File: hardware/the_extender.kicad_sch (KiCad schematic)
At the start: 122 parts, among them J0 TYPE-C 24P QT 143, J1 TYPE-C-31-M-16, J2 U231-091N-3BLRC11, J3 PJ-327D-5A, J4 PJ-327D-5A, J5 AF 10.0 HC6.3, Q4 SSM3J332R,LF, Q6 SSM3J332R,LF, U0 RT6150BGQW, U1 IP5306-I2C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

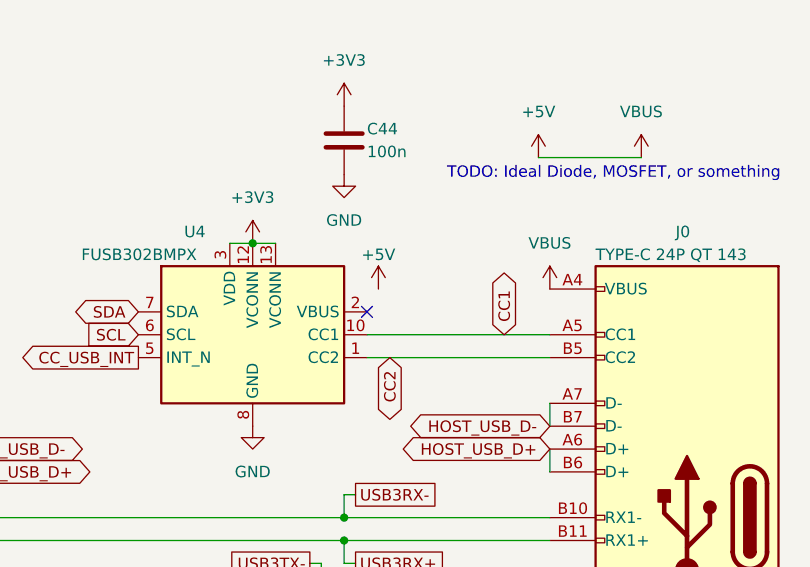
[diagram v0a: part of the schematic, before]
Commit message: reconnect VBUS to FUSB302
i think its needed for the pullups
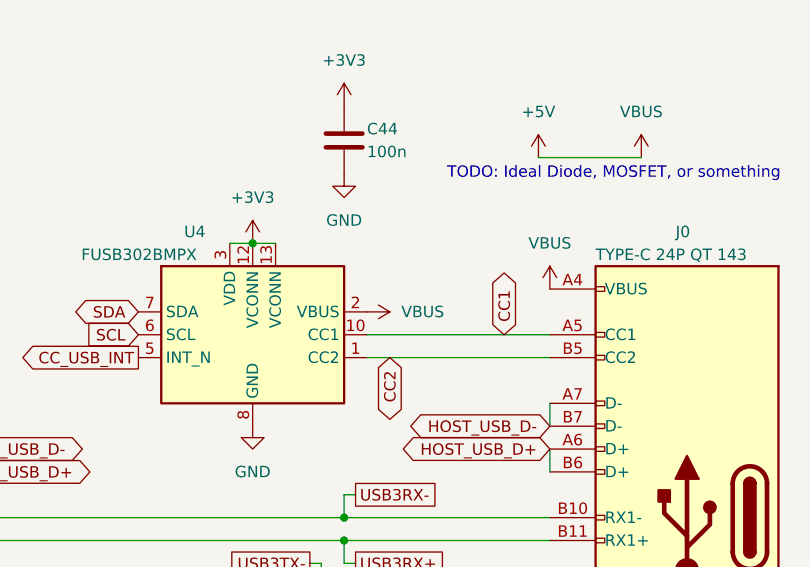
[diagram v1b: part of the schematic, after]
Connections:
- net +5V: now also U4.2 (VBUS)
- no-connect marks 50 -> 49
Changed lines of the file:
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@@
   (no_connect (at 374.65 146.05))
   (no_connect (at 60.96 137.16))
-  (no_connect (at 104.14 46.99))
   (no_connect (at 374.65 74.93))
   (no_connect (at 374.65 138.43))
@@
     )
   )
-  (symbol (lib_id "power:+5V") (at 105.41 44.45 0) (unit 1)
-    (in_bom yes) (on_board yes) (dnp no)
-    (property "Reference" "#PWR0108" (at 105.41 48.26 0)
-      (effects (font (size 1.27 1.27)) hide)
-    )
-    (property "Value" "+5V" (at 105.41 40.64 0)
-      (effects (font (size 1.27 1.27)))
-    )
-    (property "Footprint" "" (at 105.41 44.45 0)
-      (effects (font (size 1.27 1.27)) hide)
-    )
-    (property "Datasheet" "" (at 105.41 44.45 0)
-      (effects (font (size 1.27 1.27)) hide)
-    )
-    (pin "1")
-    (instances
-      (project "the_extender"
-        (path "/e63e39d7-6ac0-4ffd-8aa3-1841a4541b55"
-          (reference "#PWR0108") (unit 1)
-        )
-      )
-    )
-  )
   (symbol (lib_id "Device:R") (at 355.6 53.34 90) (unit 1)
     (in_bom yes) (on_board yes) (dnp no)
@@
         )
       )
+    )
+  )
+  (symbol (lib_id "power:VBUS") (at 104.14 46.99 270) (unit 1)
+    (in_bom yes) (on_board yes) (dnp no) (fields_autoplaced)
+    (property "Reference" "#PWR082" (at 100.33 46.99 0)
+      (effects (font (size 1.27 1.27)) hide)
+    )
+    (property "Value" "VBUS" (at 107.95 46.99 90)
+      (effects (font (size 1.27 1.27)) (justify left))
+    )
+    (property "Footprint" "" (at 104.14 46.99 0)
+      (effects (font (size 1.27 1.27)) hide)
+    )
+    (property "Datasheet" "" (at 104.14 46.99 0)
+      (effects (font (size 1.27 1.27)) hide)
+    )
+    (pin "1")
+    (instances
+      (project "the_extender"
+        (path "/e63e39d7-6ac0-4ffd-8aa3-1841a4541b55"
+          (reference "#PWR082") (unit 1)
+        )
+      )

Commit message: switch 3v3 footprint, fixup stuff
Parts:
- U0: value RT6150BGQW -> RT6150AGQW; footprint Package_SON:WSON-10-1EP_2.5x2.5mm_P0.5mm_EP1.2x2mm -> Package_DFN_QFN:WDFN-10-1EP_3x3mm_P0.5mm_EP1.8x2.5mm
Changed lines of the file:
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@@
       (effects (font (size 1.27 1.27)))
     )
-    (property "Value" "RT6150BGQW" (at 354.33 215.9 0)
+    (property "Value" "RT6150AGQW" (at 354.33 215.9 0)
       (effects (font (size 1.27 1.27)))
     )
-    (property "Footprint" "Package_SON:WSON-10-1EP_2.5x2.5mm_P0.5mm_EP1.2x2mm" (at 354.33 241.3 0)
+    (property "Footprint" "Package_DFN_QFN:WDFN-10-1EP_3x3mm_P0.5mm_EP1.8x2.5mm" (at 354.33 241.3 0)
       (effects (font (size 1.27 1.27)) hide)
     )

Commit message: switch to cheaper and smaller usb hub, part 1
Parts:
- removed R15: 12k, Resistor_SMD:R_0805_2012Metric_Pad1.20x1.40mm_HandSolder, symbol Device:R
- removed R17, R33: 10k, Resistor_SMD:R_0805_2012Metric_Pad1.20x1.40mm_HandSolder, symbol Device:R
- removed U5: USB2514B_Bi, Package_DFN_QFN:QFN-36-1EP_6x6mm_P0.5mm_EP3.7x3.7mm, symbol Interface_USB:USB2514B_Bi
- added JP2, JP3: SolderJumper_2_Open, symbol Jumper:SolderJumper_2_Open
- added U5: ~, Package_DFN_QFN:QFN-24-1EP_4x4mm_P0.5mm_EP2.6x2.6mm, symbol H3_IC:CH334F
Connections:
- net +3.3VP: now also C13.2, C14.2, JP3.1 (A), U5.20 (3V3)
- net CLK_24M: no longer U2.29 (GPIO18)
- net EXT_USB_D+: now also U5.8 (DP3)
- net EXT_USB_D-: now also U5.7 (DN3)
- net GND: now also JP2.1 (A), U5.0 (GND)
- net HOST_USB_D+: now also U5.15 (DPU)
- net HOST_USB_D-: now also U5.14 (DNU)
- net HUB_SCL: now also U5.13 (LED3/SCL)
- net HUB_SDA: now also U5.21 (LED4/SDA)
- net MCU_USB_D+: now also U5.10 (DP2)
- net MCU_USB_D-: now also U5.9 (DN2)
- net SND_USB_D+: now also U5.12 (DP1)
- net SND_USB_D-: now also U5.11 (DN1)
- net STOR_USB_D+: now also U5.6 (DP4)
- net STOR_USB_D-: now also U5.5 (DN4)
- new net: JP3.2 (B), U5.19 (V5)
- new net CLK_12M: JP2.2 (B), U2.29 (GPIO18), U5.4 (XI)
- no-connect marks 49 -> 39
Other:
- moved on the sheet: C13, C14

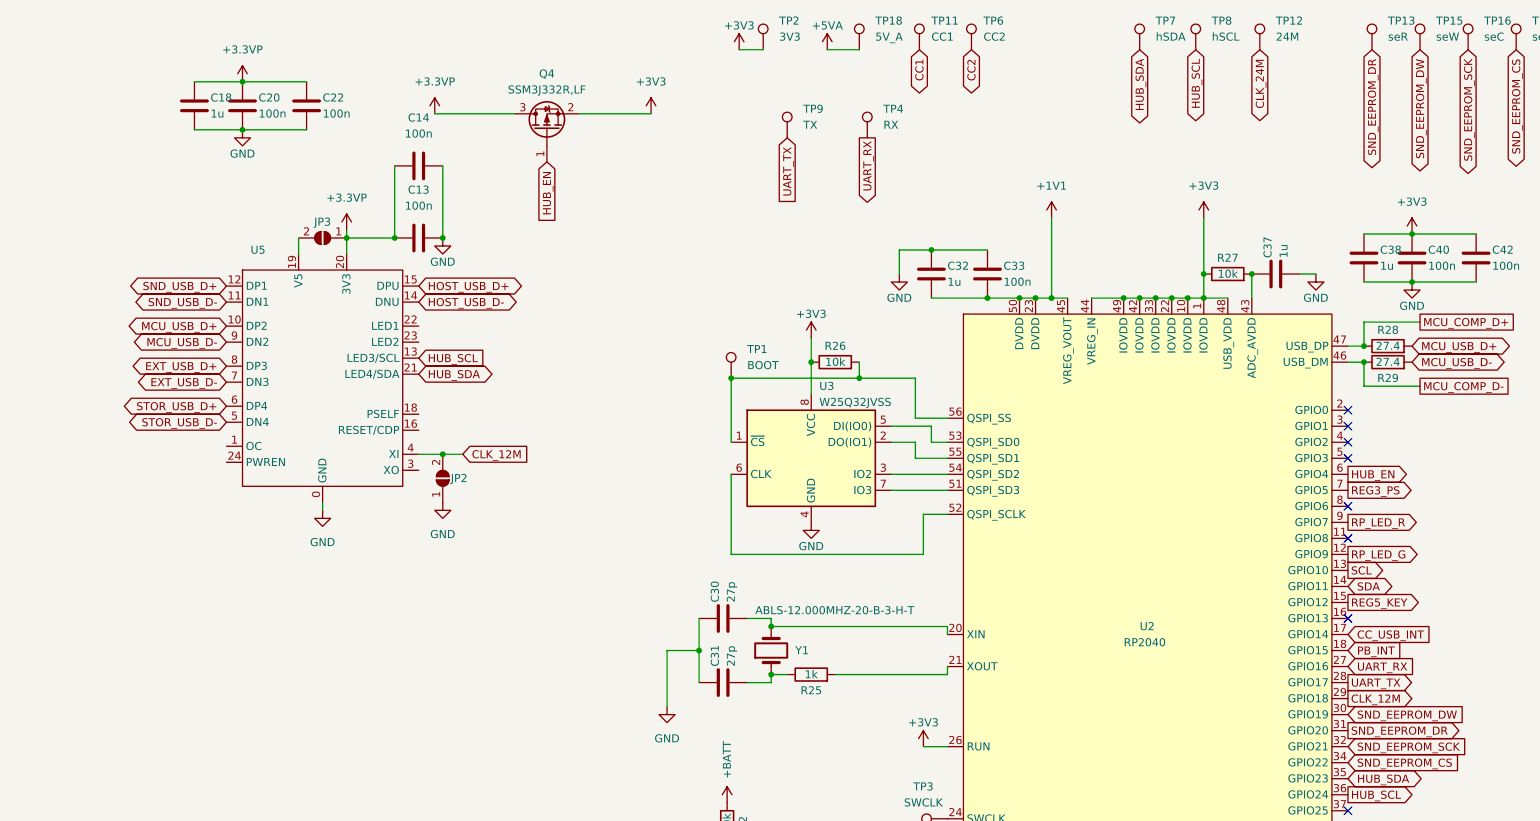
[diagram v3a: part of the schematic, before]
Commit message: switch usb hub, part 2: PCB
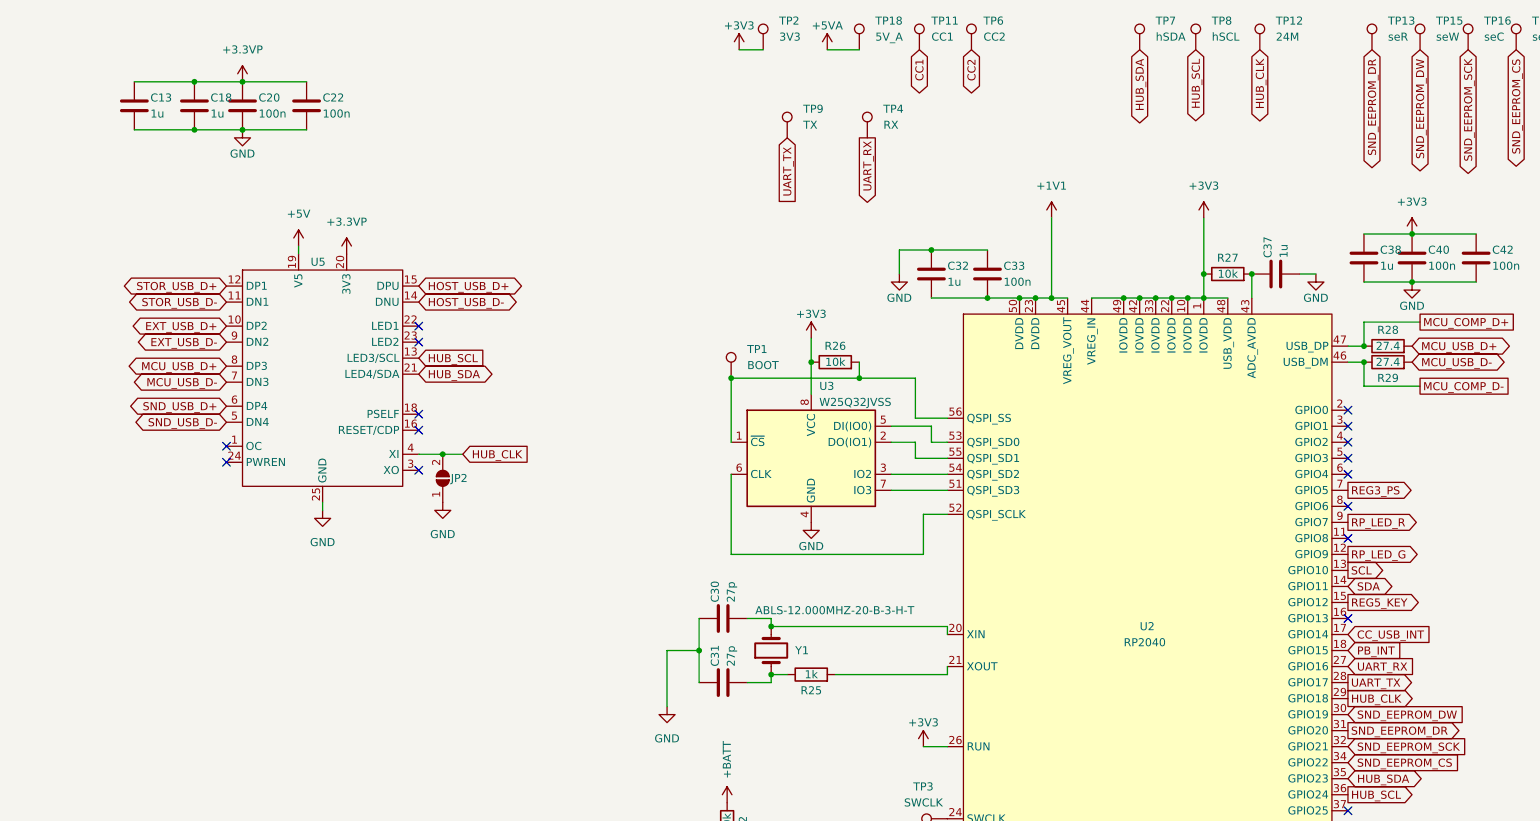
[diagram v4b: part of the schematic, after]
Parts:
- removed C14: 100n, Capacitor_SMD:C_0805_2012Metric_Pad1.18x1.45mm_HandSolder, symbol Device:C
- removed JP3: SolderJumper_2_Open, symbol Jumper:SolderJumper_2_Open
- removed Q4: SSM3J332R,LF, Package_TO_SOT_SMD:SOT-23_Handsoldering, symbol Device:Q_PMOS_GSD
- C13: value 100n -> 1u
- JP2: footprint (none) -> Jumper:SolderJumper-2_P1.3mm_Open_TrianglePad1.0x1.5mm
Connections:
- net CLK_24M is gone; now on net HUB_CLK: TP12.1
- net +3.3VP: now also C13.1; no longer C13.2
- net +5V: now also U5.19 (V5)
- net EXT_USB_D+: now also U5.10 (DP2); no longer U5.8 (DP3)
- net EXT_USB_D-: now also U5.9 (DN2); no longer U5.7 (DN3)
- net GND: now also C13.2, U5.25 (GND); no longer C13.1, U5.0 (GND)
- net MCU_USB_D+: now also U5.8 (DP3); no longer U5.10 (DP2)
- net MCU_USB_D-: now also U5.7 (DN3); no longer U5.9 (DN2)
- net SND_USB_D+: now also U5.6 (DP4); no longer U5.12 (DP1)
- net SND_USB_D-: now also U5.5 (DN4); no longer U5.11 (DN1)
- net STOR_USB_D+: now also U5.12 (DP1); no longer U5.6 (DP4)
- net STOR_USB_D-: now also U5.11 (DN1); no longer U5.5 (DN4)
- net CLK_12M renamed HUB_CLK
- net HUB_EN: no longer names the net of U2.6 (GPIO4)
- no-connect marks 39 -> 47

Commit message: small fixes
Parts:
- TP12: value 24M -> hCLK
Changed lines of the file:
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@@
   (symbol (lib_id "Connector:TestPoint") (at 360.68 17.78 0) (unit 1)
     (in_bom yes) (on_board yes) (dnp no) (fields_autoplaced)
-    (property "Reference" "TP12" (at 363.22 13.2079 0)
+    (property "Reference" "TP12" (at 363.22 13.208 0)
       (effects (font (size 1.27 1.27)) (justify left))
     )
-    (property "Value" "24M" (at 363.22 15.7479 0)
+    (property "Value" "hCLK" (at 363.22 15.748 0)
       (effects (font (size 1.27 1.27)) (justify left))
     )

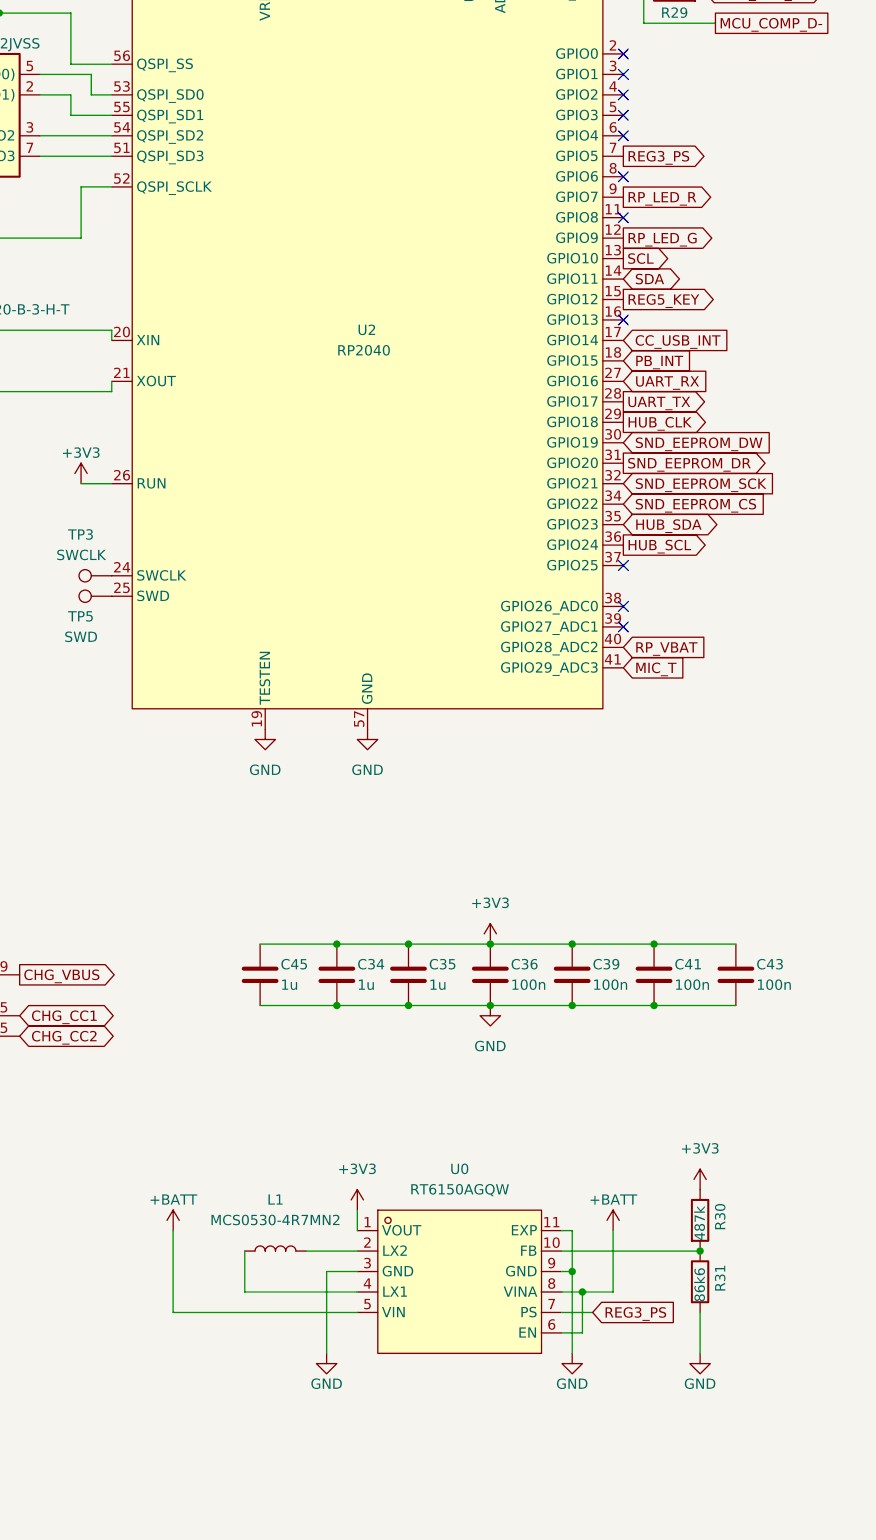
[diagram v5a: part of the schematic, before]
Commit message: Switch to linear LDO Regulator to decrease cost
might also improve ADC accuracy...
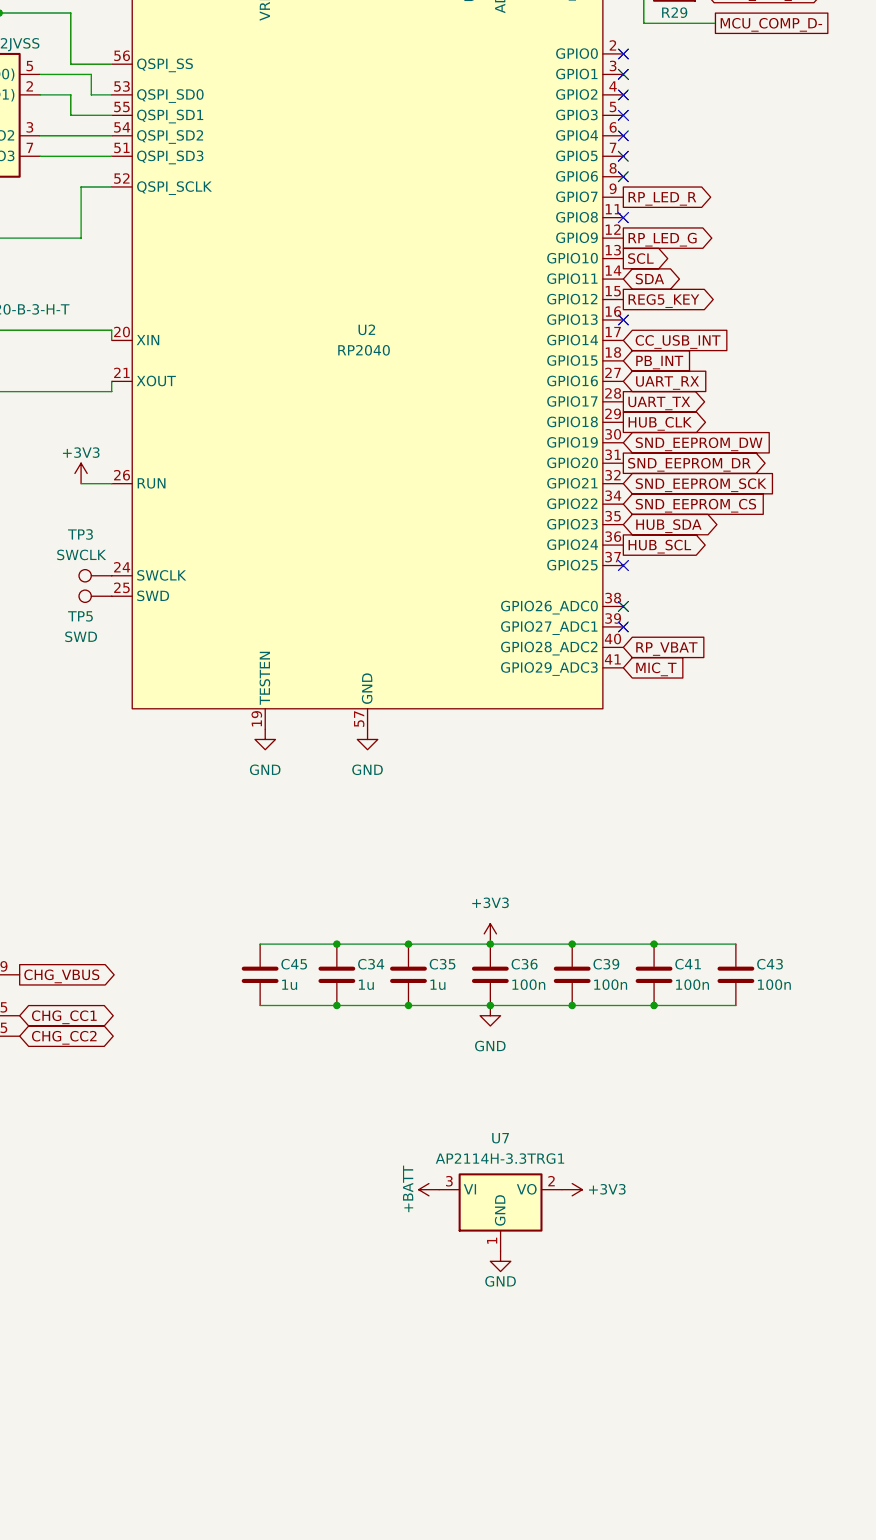
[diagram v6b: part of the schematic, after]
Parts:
- removed L1: MCS0530-4R7MN2, easyeda2kicad:IND-SMD_L5.2-W5.2_YSPI0530, symbol Device:L
- removed R30: 487k, Resistor_SMD:R_0805_2012Metric_Pad1.20x1.40mm_HandSolder, symbol Device:R
- removed R31: 86k6, Resistor_SMD:R_0805_2012Metric_Pad1.20x1.40mm_HandSolder, symbol Device:R
- removed U0: RT6150AGQW, Package_DFN_QFN:WDFN-10-1EP_3x3mm_P0.5mm_EP1.8x2.5mm, symbol LCSC:RT6150BGQW
- added U7: AP2114H-3.3TRG1, Package_TO_SOT_SMD:SOT-223-3_TabPin2, symbol Regulator_Linear:AMS1117-3.3
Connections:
- net +3V3: now also U7.2 (VO)
- net +BATT: now also U7.3 (VI)
- net GND: now also U7.1 (GND)
- net REG3_PS: no longer names the net of U2.7 (GPIO5)
- no-connect marks 47 -> 48

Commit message: oh, this belongs to an earlier commit
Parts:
- removed C45: 1u, Capacitor_SMD:C_0805_2012Metric_Pad1.18x1.45mm_HandSolder, symbol Device:C
- added C14: 22u, Capacitor_SMD:C_1206_3216Metric_Pad1.33x1.80mm_HandSolder, symbol Device:C
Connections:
- net +3V3: now also C14.1
- net GND: now also C14.2
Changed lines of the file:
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@@
     )
   )
+  (symbol (lib_id "Device:C") (at 329.565 189.23 0) (unit 1)
+    (in_bom yes) (on_board yes) (dnp no)
+    (property "Reference" "C14" (at 332.105 187.96 0)
+      (effects (font (size 1.27 1.27)) (justify left))
+    )
+    (property "Value" "22u" (at 332.105 190.5 0)
+      (effects (font (size 1.27 1.27)) (justify left))
+    )
+    (property "Footprint" "Capacitor_SMD:C_1206_3216Metric_Pad1.33x1.80mm_HandSolder" (at 330.5302 193.04 0)
+      (effects (font (size 1.27 1.27)) hide)
+    )
+    (property "Datasheet" "~" (at 329.565 189.23 0)
+      (effects (font (size 1.27 1.27)) hide)
+    )
+    (pin "1")
+    (pin "2")
+    (instances
+      (project "the_extender"
+        (path "/e63e39d7-6ac0-4ffd-8aa3-1841a4541b55"
+          (reference "C14") (unit 1)
+        )
+      )
+    )
+  )
   (symbol (lib_id "Device:C") (at 170.18 208.28 0) (unit 1)
     (in_bom yes) (on_board yes) (dnp no)
@@
         )
       )
-    )
-  )
-  (symbol (lib_id "Device:C") (at 329.565 189.23 0) (unit 1)
-    (in_bom yes) (on_board yes) (dnp no)
-    (property "Reference" "C45" (at 332.105 187.96 0)
-      (effects (font (size 1.27 1.27)) (justify left))
-    )
-    (property "Value" "1u" (at 332.105 190.5 0)
-      (effects (font (size 1.27 1.27)) (justify left))
-    )
-    (property "Footprint" "Capacitor_SMD:C_0805_2012Metric_Pad1.18x1.45mm_HandSolder" (at 330.5302 193.04 0)
-      (effects (font (size 1.27 1.27)) hide)
-    )
-    (property "Datasheet" "~" (at 329.565 189.23 0)
-      (effects (font (size 1.27 1.27)) hide)
-    )
-    (pin "1")
-    (pin "2")
-    (instances
-      (project "the_extender"
-        (path "/e63e39d7-6ac0-4ffd-8aa3-1841a4541b55"
-          (reference "C45") (unit 1)
-        )
-      )
